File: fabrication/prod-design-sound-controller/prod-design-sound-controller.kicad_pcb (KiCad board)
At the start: 2 copper layers, 167.2 x 110 mm, 25 parts, among them SW1 BYPASS-SWITCH, U7 LEFT-TRIGGER, U8 RIGHT-TRIGGER

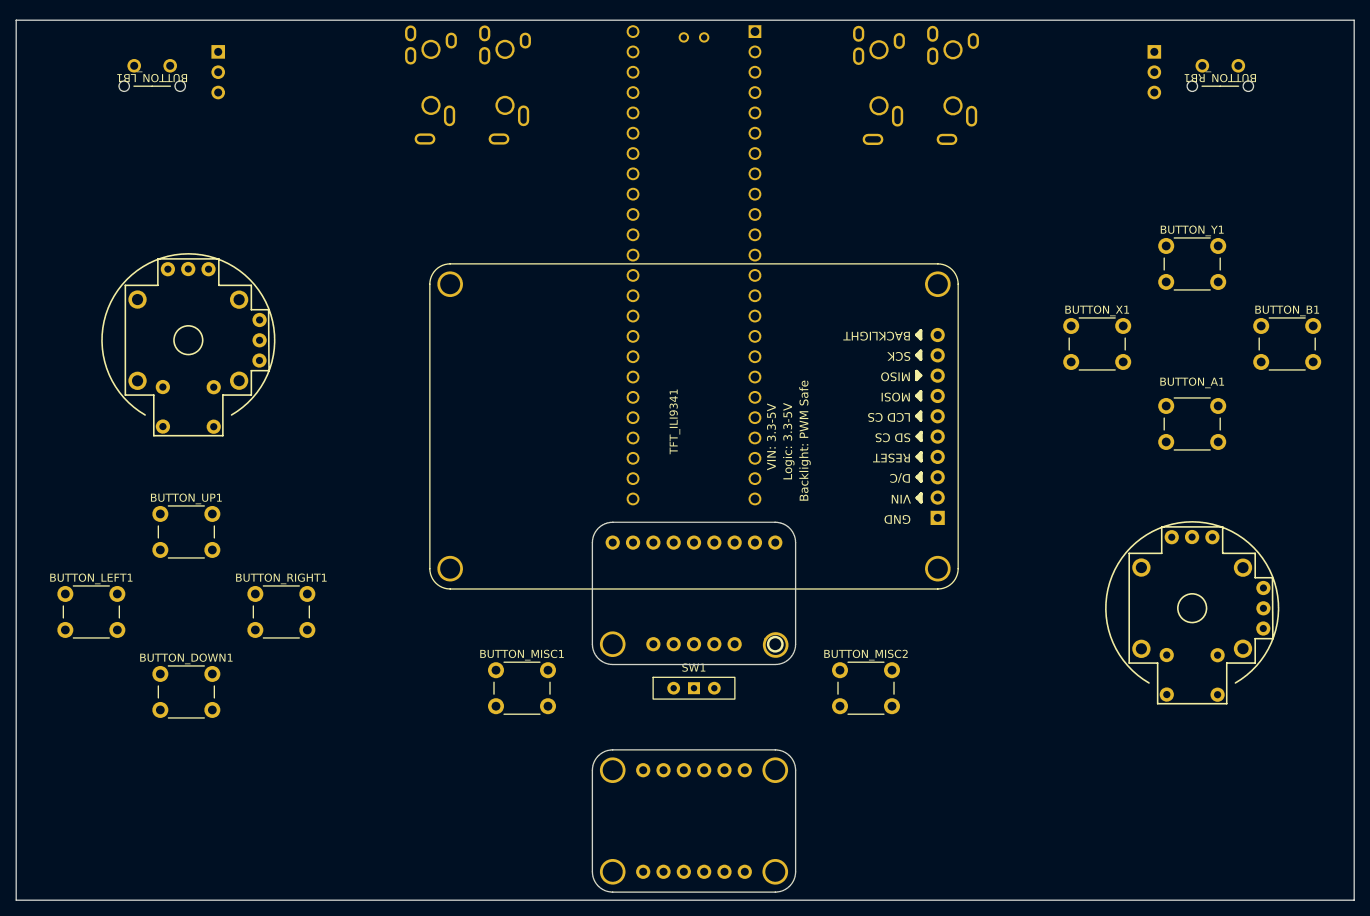
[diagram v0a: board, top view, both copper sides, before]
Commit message: basic tinyusb test, transitioning to pio branch
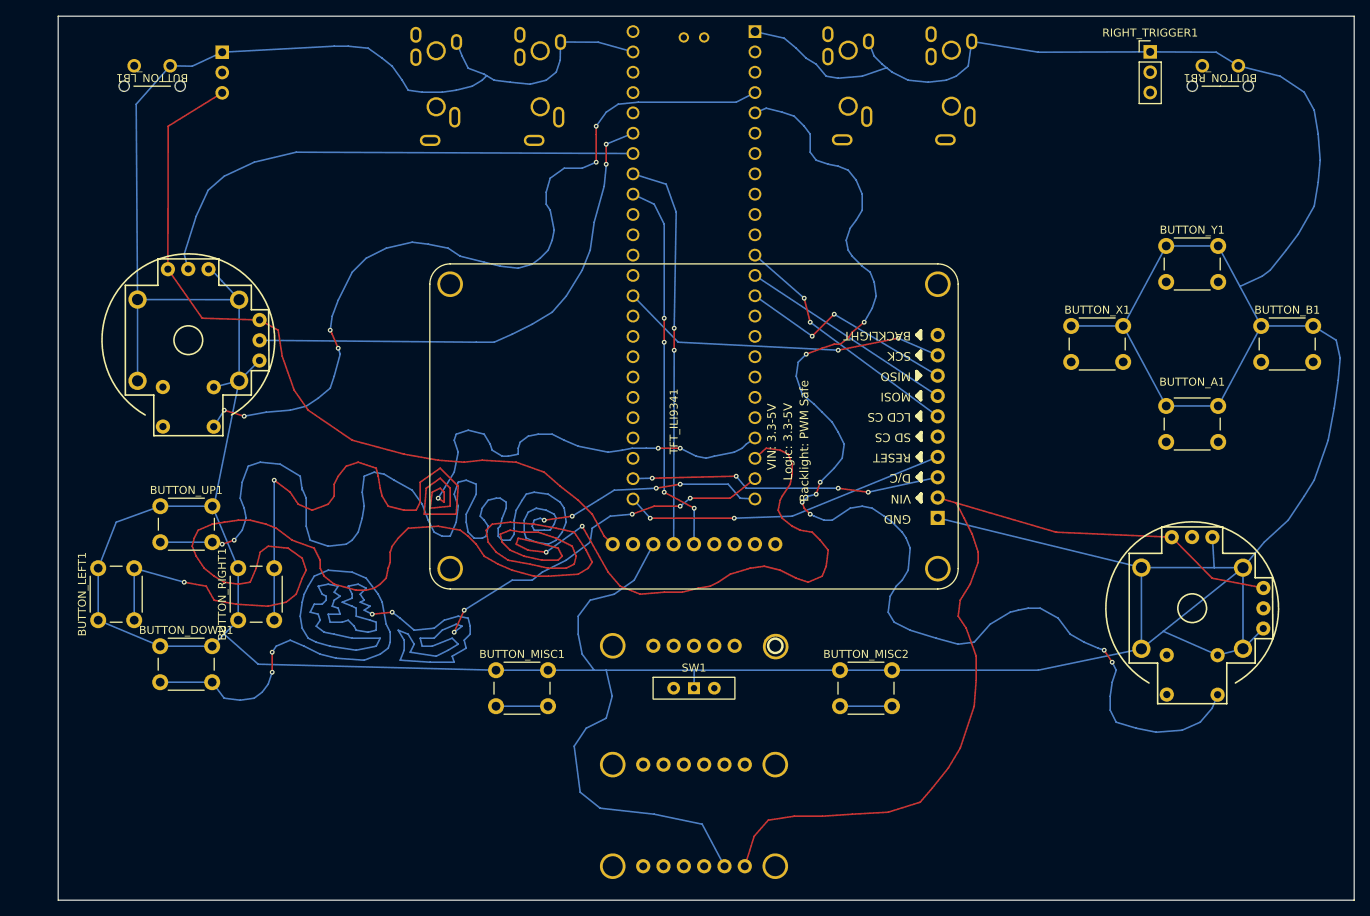
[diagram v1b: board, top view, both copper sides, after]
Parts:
- removed U7: LEFT-TRIGGER, Connector_PinHeader_2.54mm:PinHeader_1x03_P2.54mm_Vertical
- removed U8: RIGHT-TRIGGER, Connector_PinHeader_2.54mm:PinHeader_1x03_P2.54mm_Vertical
- added LEFT_TRIGGER1: ~, Connector_PinHeader_2.54mm:PinHeader_1x03_P2.54mm_Vertical, B.Cu at (90.5, 20.0)
- added RIGHT_TRIGGER1: ~, Connector_PinHeader_2.54mm:PinHeader_1x03_P2.54mm_Vertical, F.Cu at (206.5, 20.0)
- moved AUDIO_JACK1 64.6 mm to (117.2, 23.7)
- moved AUDIO_JACK3 55.8 mm to (181.7, 23.6)
- moved AUDIO_JACK4 52.2 mm to (168.8, 23.6)
- moved AUDIO_JACK2 42.3 mm to (130.2, 23.7)
- moved BUTTON_LEFT1 5.26 mm to (75.0, 91.0), turned to 90 degrees
- moved BUTTON_RIGHT1 3.92 mm to (92.5, 91.0), turned to 90 degrees
- moved BUTTON_DOWN1 3.47 mm to (82.8, 94.2)
- moved LSM6DSOX_GYRO1 3.30 mm to (149.7, 100.8)
- moved BUTTON_UP1 0.97 mm to (82.8, 76.8)
- moved MCP4728_DAC1 0.70 mm to (149.6, 101.9)
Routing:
- net GND: track 0.00 -> 712.9 mm
- net BUTTON-LEFT: track 0.00 -> 242.2 mm, vias 0 -> 3
- net BUTTON-DOWN: track 0.00 -> 220.1 mm, vias 0 -> 9
- net +3.3V: track 0.00 -> 208.2 mm
- net BUTTON-UP: track 0.00 -> 157.7 mm, vias 0 -> 6
- net RIGHT-JOY-SEL: track 0.00 -> 151.7 mm, vias 0 -> 8
- net BUTTON-RIGHT: track 0.00 -> 129.8 mm, vias 0 -> 4
- net LEFT-JOY-SEL: track 0.00 -> 100.6 mm, vias 0 -> 6
- net LEFT-JOY-X: track 0.00 -> 64.8 mm
- net LEFT-JOY-Y: track 0.00 -> 63.8 mm, vias 0 -> 2
- net WIRE1-SCL: track 0.00 -> 49.6 mm, vias 0 -> 2
- net WIRE1-SDA: track 0.00 -> 48.5 mm, vias 0 -> 4
- net ILI9341-DISPLAY-SCK: track 0.00 -> 41.1 mm, vias 0 -> 2
- net ILI9341-DISPLAY-RST: track 0.00 -> 40.6 mm, vias 0 -> 2
- net ILI9341-DISPLAY-DC: track 0.00 -> 39.0 mm, vias 0 -> 4
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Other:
- board size 167.2 x 110 mm -> 162 x 110.5 mm
